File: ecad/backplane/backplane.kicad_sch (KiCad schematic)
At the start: 25 parts, among them J1 10145891-0320J13LF, J2 10145891-0320J13LF, J3 10145891-0320J13LF, J4 10145891-0320J13LF, J5 USB4105-GF-A, J6 5017868090, U1 MCP16331x-xCH

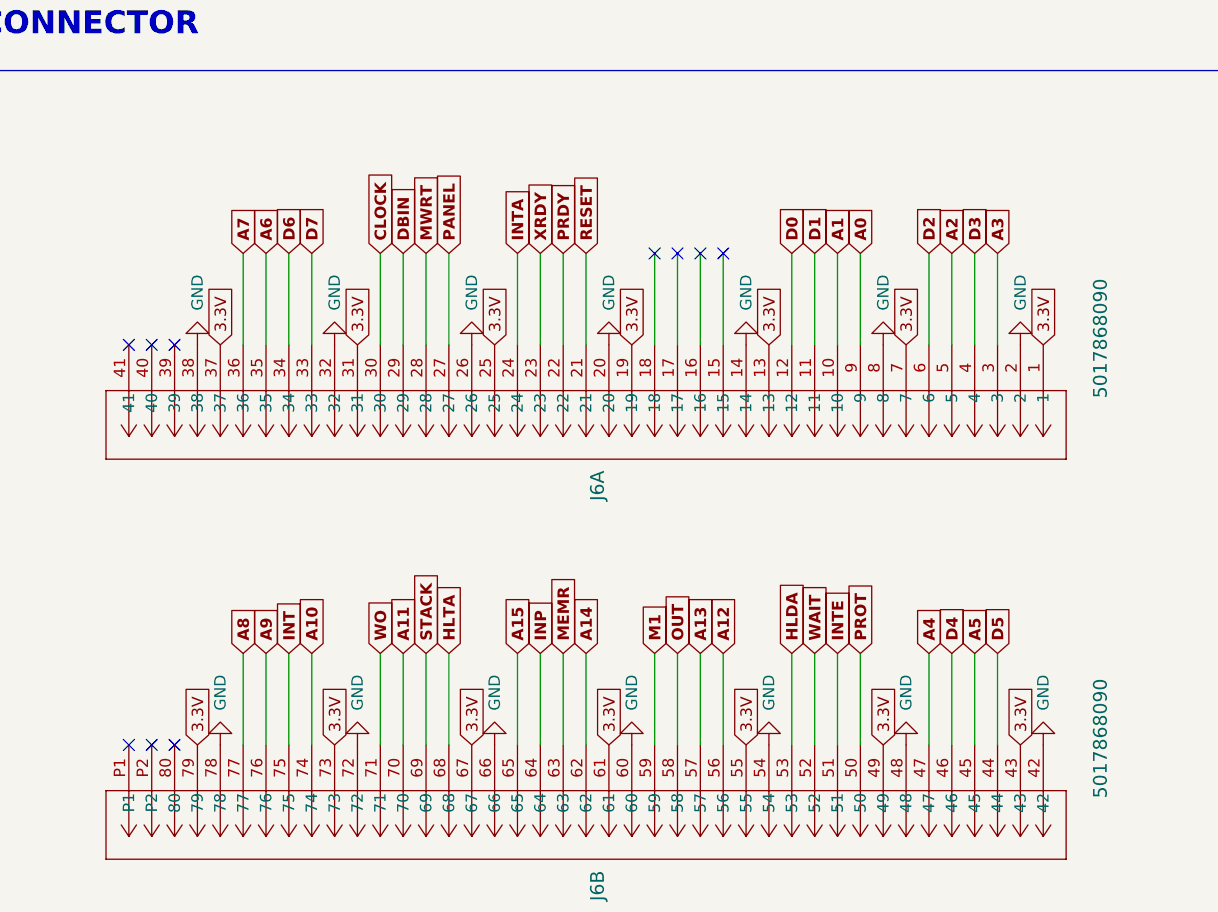
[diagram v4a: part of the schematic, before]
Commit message: backplane reverse FFC wiring
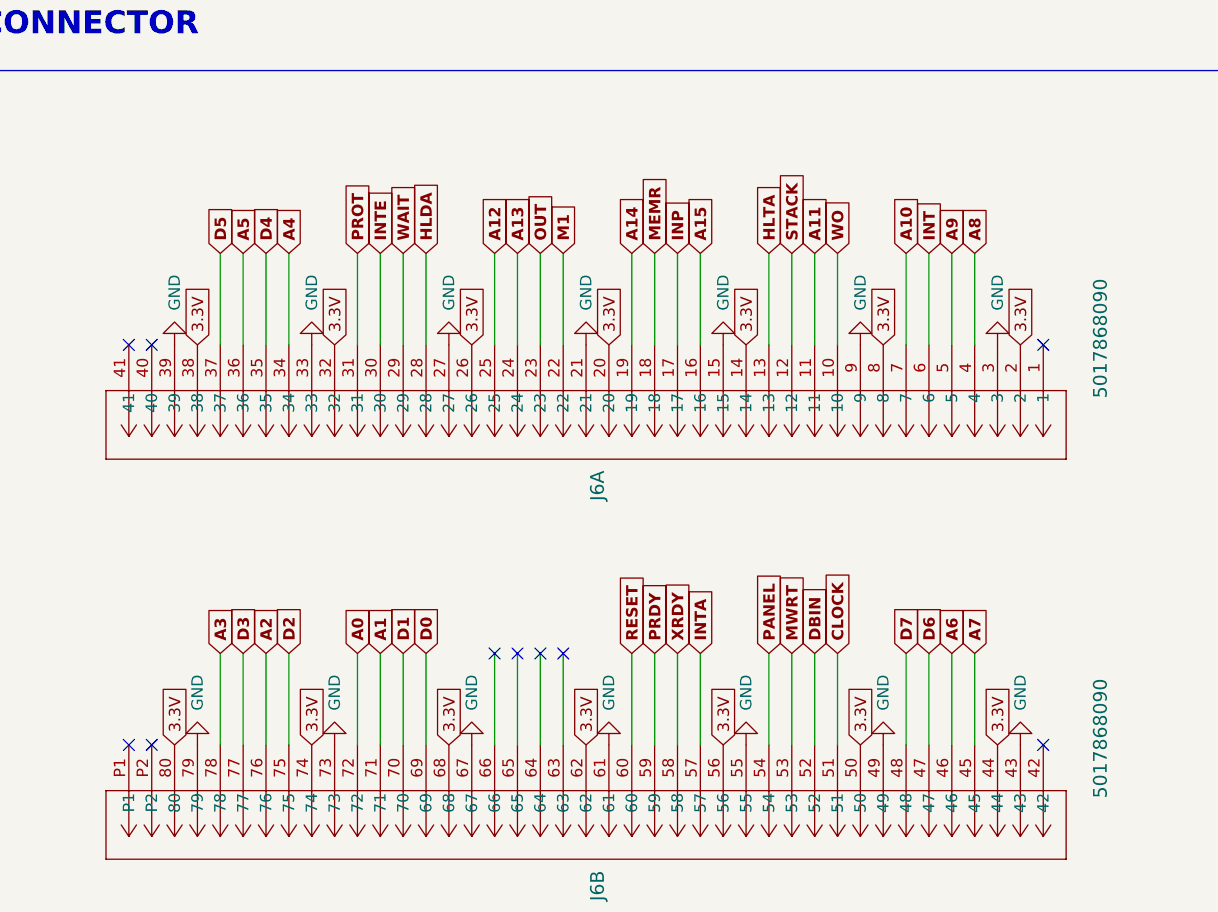
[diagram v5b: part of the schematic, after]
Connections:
- net 3.3V: now also J6.14, J6.2, J6.20, J6.26, J6.32, J6.38, J6.44, J6.50, J6.56, J6.62, J6.68, J6.74, J6.8, J6.80; no longer J6.1, J6.13, J6.19, J6.25, J6.31, J6.37, J6.43, J6.49, J6.55, J6.61, J6.67, J6.7, J6.73, J6.79
- net A0: now also J6.72; no longer J6.9
- net A1: now also J6.71; no longer J6.10
- net A10: now also J6.7; no longer J6.74
- net A11: now also J6.11; no longer J6.70
- net A12: now also J6.25; no longer J6.56
- net A13: now also J6.24; no longer J6.57
- net A14: now also J6.19; no longer J6.62
- net A15: now also J6.16; no longer J6.65
- net A2: now also J6.76; no longer J6.5
- net A3: now also J6.78; no longer J6.3
- net A4: now also J6.34; no longer J6.47
- net A5: now also J6.36; no longer J6.45
- net A6: now also J6.46; no longer J6.35
- net A7: now also J6.45; no longer J6.36
- net A8: now also J6.4; no longer J6.77
- net A9: now also J6.5; no longer J6.76
- net CLOCK: now also J6.51; no longer J6.30
- net D0: now also J6.69; no longer J6.12
- net D1: now also J6.70; no longer J6.11
- net D2: now also J6.75; no longer J6.6
- net D3: now also J6.77; no longer J6.4
- net D4: now also J6.35; no longer J6.46
- net D5: now also J6.37; no longer J6.44
- net D6: now also J6.47; no longer J6.34
- net D7: now also J6.48; no longer J6.33
- net DBIN: now also J6.52; no longer J6.29
- net GND: now also J6.15, J6.21, J6.27, J6.3, J6.33, J6.39, J6.43, J6.49, J6.55, J6.61, J6.67, J6.73, J6.79, J6.9; no longer J6.14, J6.2, J6.20, J6.26, J6.32, J6.38, J6.42, J6.48, J6.54, J6.60, J6.66, J6.72, J6.78, J6.8
- net HLDA: now also J6.28; no longer J6.53
- net HLTA: now also J6.13; no longer J6.68
- net INP: now also J6.17; no longer J6.64
- net INT: now also J6.6; no longer J6.75
- net INTA: now also J6.57; no longer J6.24
- net INTE: now also J6.30; no longer J6.51
- net M1: now also J6.22; no longer J6.59
- net MEMR: now also J6.18; no longer J6.63
- net MWRT: now also J6.53; no longer J6.28
- net OUT: now also J6.23; no longer J6.58
- net PANEL: now also J6.54; no longer J6.27
- net PRDY: now also J6.59; no longer J6.22
- net PROT: now also J6.31; no longer J6.50
- net RESET: now also J6.60; no longer J6.21
- net STACK: now also J6.12; no longer J6.69
- net WAIT: now also J6.29; no longer J6.52
- net WO: now also J6.10; no longer J6.71
- net XRDY: now also J6.58; no longer J6.23
